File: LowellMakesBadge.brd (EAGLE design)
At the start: 50 x 50 mm, 15 parts

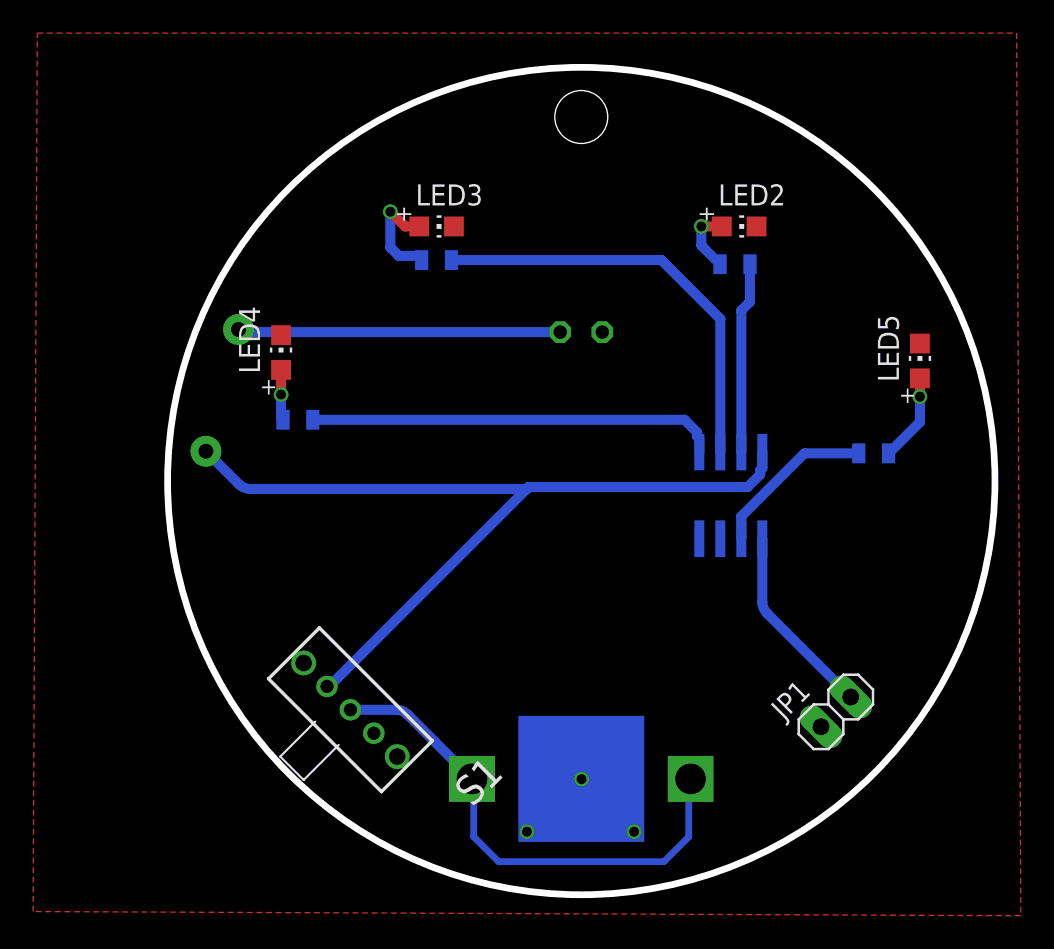
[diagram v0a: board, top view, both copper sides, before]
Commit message: Updates to use all at tiny pins (last GPIO to control main through hole LED as well
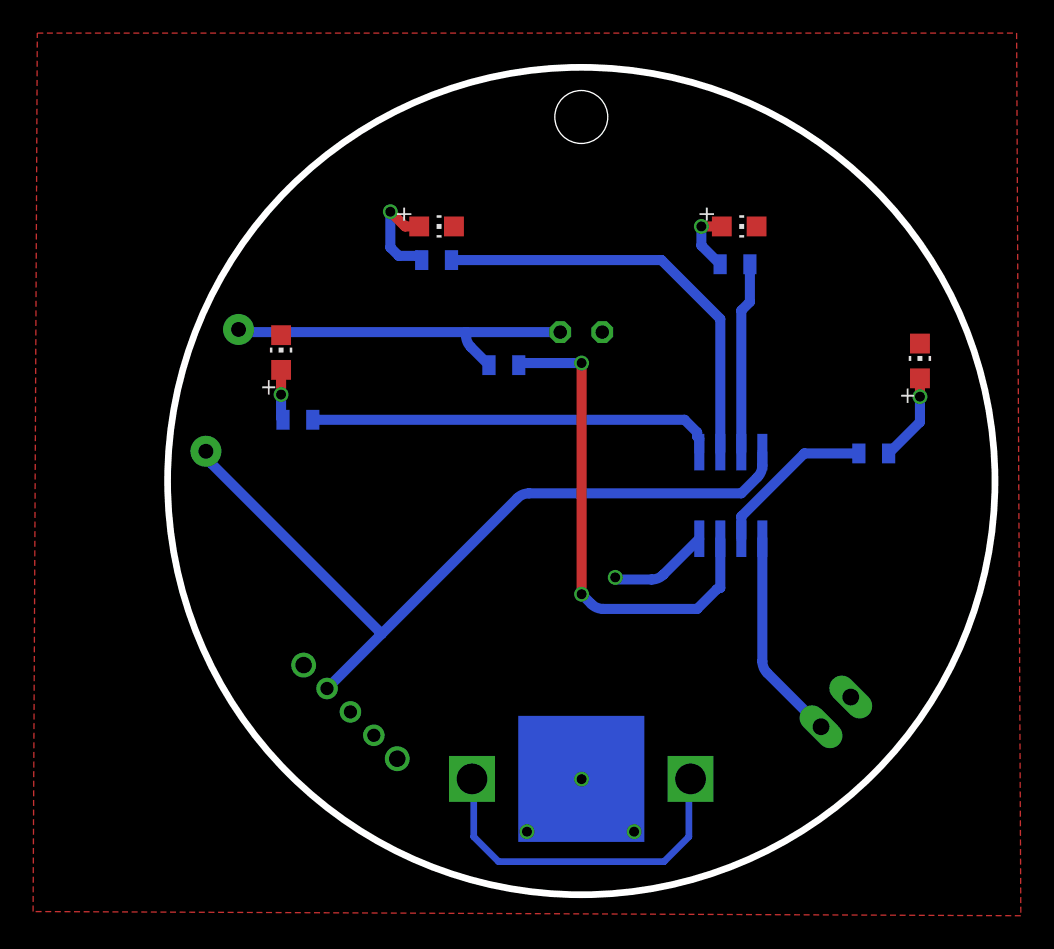
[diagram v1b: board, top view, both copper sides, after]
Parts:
- added R6: (no value), SparkFun:0805
- moved S1 0.13 mm to (11.0, 11.0), flipped to the bottom, turned to 135 degrees
- flipped JP1 to the bottom, turned to 315 degrees
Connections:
- new net N$14: R6.2, U$2.3
- net N$1: now also R6.1
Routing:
- net N$14: track 0.00 -> 30.0 mm, vias 0 -> 2
- net BATT: track 9.01 -> 0.00 mm
- net GND: track 0.00 -> 6.04 mm, vias 0 -> 4
- net VCC: track 53.1 -> 48.2 mm
- net N$1: track 19.5 -> 22.0 mm
- net RST: track 11.7 -> 12.8 mm

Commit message: Updates to wire in a full programming header.  moved SMD led pins around to simplify routing
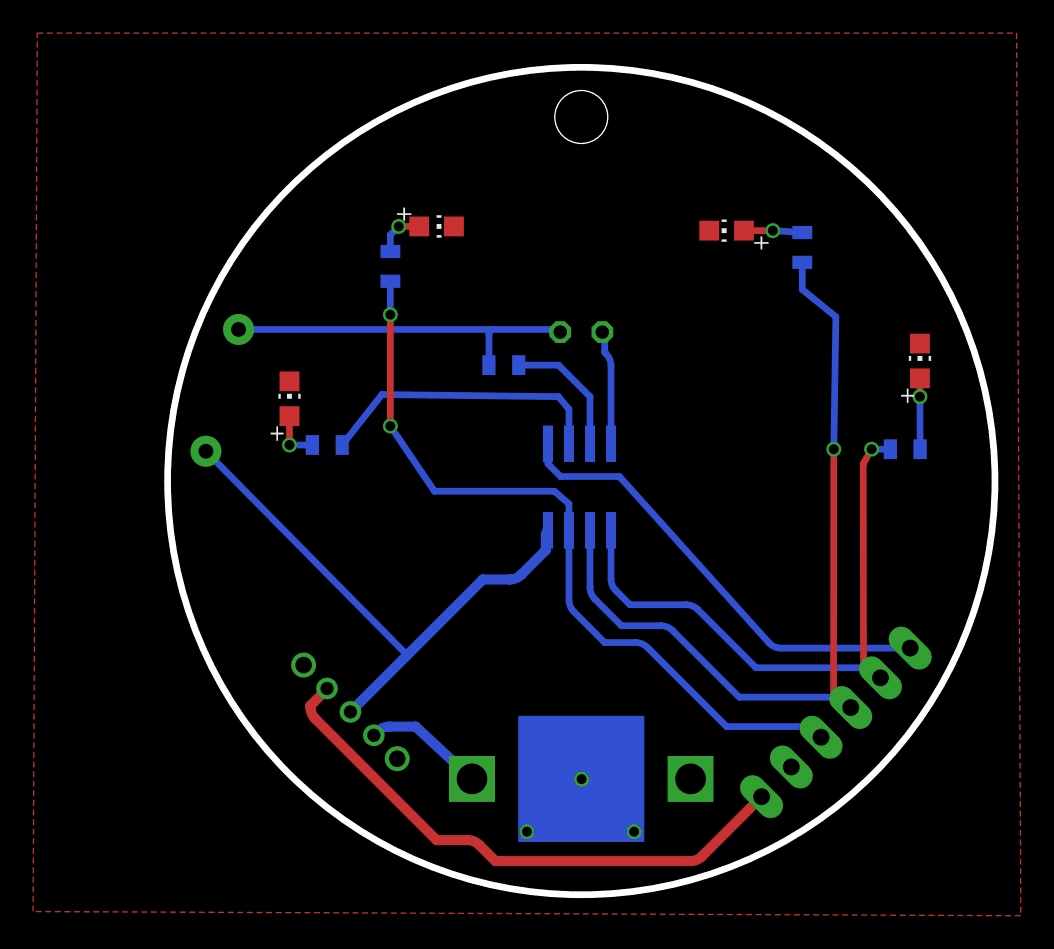
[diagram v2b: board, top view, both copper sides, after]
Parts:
- removed JP1: (no value), pinhead:1X02
- added JP2: (no value), pinhead:1X06
- moved R4 32.2 mm to (38.4, 39.1), turned to 90 degrees
- moved LED2 29.1 mm to (7.37, 30.0), turned to 0 degrees
- moved LED4 27.9 mm to (33.8, 40.1), turned to 90 degrees
- moved R2 27.0 mm to (9.65, 27.2)
- moved U$2 9.16 mm to (24.9, 24.6), turned to 180 degrees
- moved R3 2.82 mm to (13.5, 38.0), turned to 90 degrees
- moved R5 1.92 mm to (44.6, 26.9), turned to 180 degrees
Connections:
- removed net N$6 (its old number): R3.1, U$2.6
- removed net N$7: R2.1, U$2.7
- removed net N$8: R5.2, U$2.2
- removed net N$9: LED5.A, R5.1
- removed net RST: JP1.2, U$2.1
- new net N$4: LED5.A, R5.2
- new net PB0/MOSI: JP2.2, R5.1, U$2.5
- new net PB1/MISO: JP2.3, R4.1, U$2.6
- new net PB2/SCK: JP2.4, R3.1, U$2.7
- new net PROG_VCC: JP2.6, S1.3
- new net RESET: JP2.1, U$2.1
- net BATT: now also S1.1; no longer S1.2
- net GND: now also JP2.5; no longer JP1.1
- net N$5: now also R2.1, U$2.2; no longer R4.1, U$2.5
- net VCC: now also S1.2; no longer S1.3
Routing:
- net PB1/MISO: track 0.00 -> 50.7 mm, vias 0 -> 1
- net PB2/SCK: track 0.00 -> 46.4 mm, vias 0 -> 2
- net PB0/MOSI: track 0.00 -> 37.4 mm, vias 0 -> 1
- net PROG_VCC: track 0.00 -> 34.3 mm
- net RESET: track 0.00 -> 28.3 mm
- net N$6 (its old number): track 25.8 -> 0.00 mm
- net N$3: track 30.0 -> 7.94 mm, vias 2 -> 0
- net N$2: track 21.2 -> 0.00 mm
- net VCC: track 48.2 -> 34.3 mm
- net RST: track 12.8 -> 0.00 mm
- net N$7: track 11.6 -> 0.00 mm
- net N$8: track 10.0 -> 0.00 mm
- net BATT: track 0.00 -> 7.33 mm
- net N$5: track 24.8 -> 17.6 mm
- net N$9: track 5.32 -> 0.00 mm, vias 1 -> 0
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
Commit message: Cleaned up the battery power signal and passed some DRC tests
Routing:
- net N$2: track 0.00 -> 20.5 mm
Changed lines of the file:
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@@
 <wire x1="45.466" y1="30.099" x2="45.466" y2="31.208" width="0.4064" layer="1"/>
+</signal>
+<signal name="N$2">
+<wire x1="31.623" y1="6.858" x2="31.623" y2="3.9702125" width="0.6096" layer="16"/>
+<wire x1="31.623" y1="3.9702125" x2="31.33010625" y2="3.26310625" width="0.6096" layer="16" curve="-45"/>
+<wire x1="31.33010625" y1="3.26310625" x2="30.099" y2="2.032" width="0.6096" layer="16"/>
+<wire x1="30.099" y1="2.032" x2="20.0992125" y2="2.032" width="0.6096" layer="16"/>
+<wire x1="20.0992125" y1="2.032" x2="19.39210625" y2="2.32489375" width="0.6096" layer="16" curve="-45"/>
+<wire x1="19.39210625" y1="2.32489375" x2="18.288" y2="3.429" width="0.6096" layer="16"/>
+<wire x1="18.288" y1="3.429" x2="18.288" y2="6.223" width="0.6096" layer="16"/>
 </signal>
 </signals>

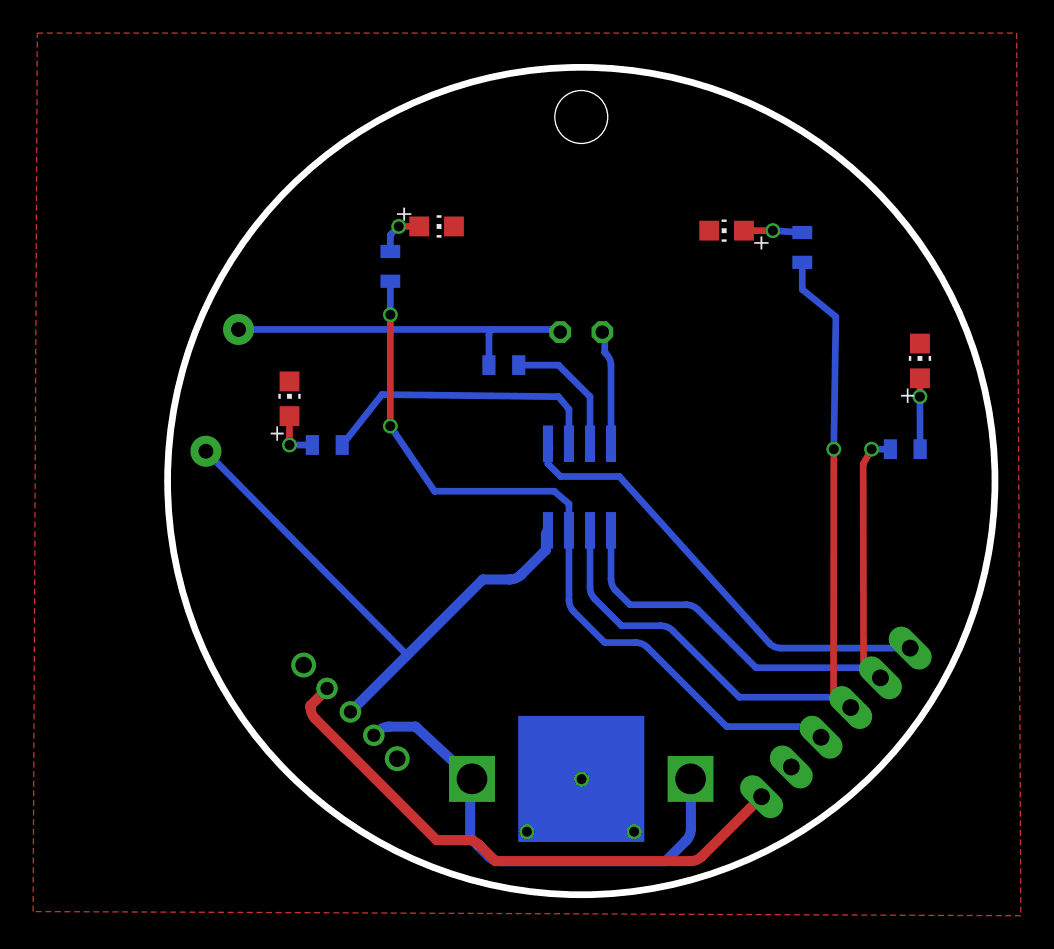
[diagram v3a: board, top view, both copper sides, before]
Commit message: Update to make board render properly in 3d model
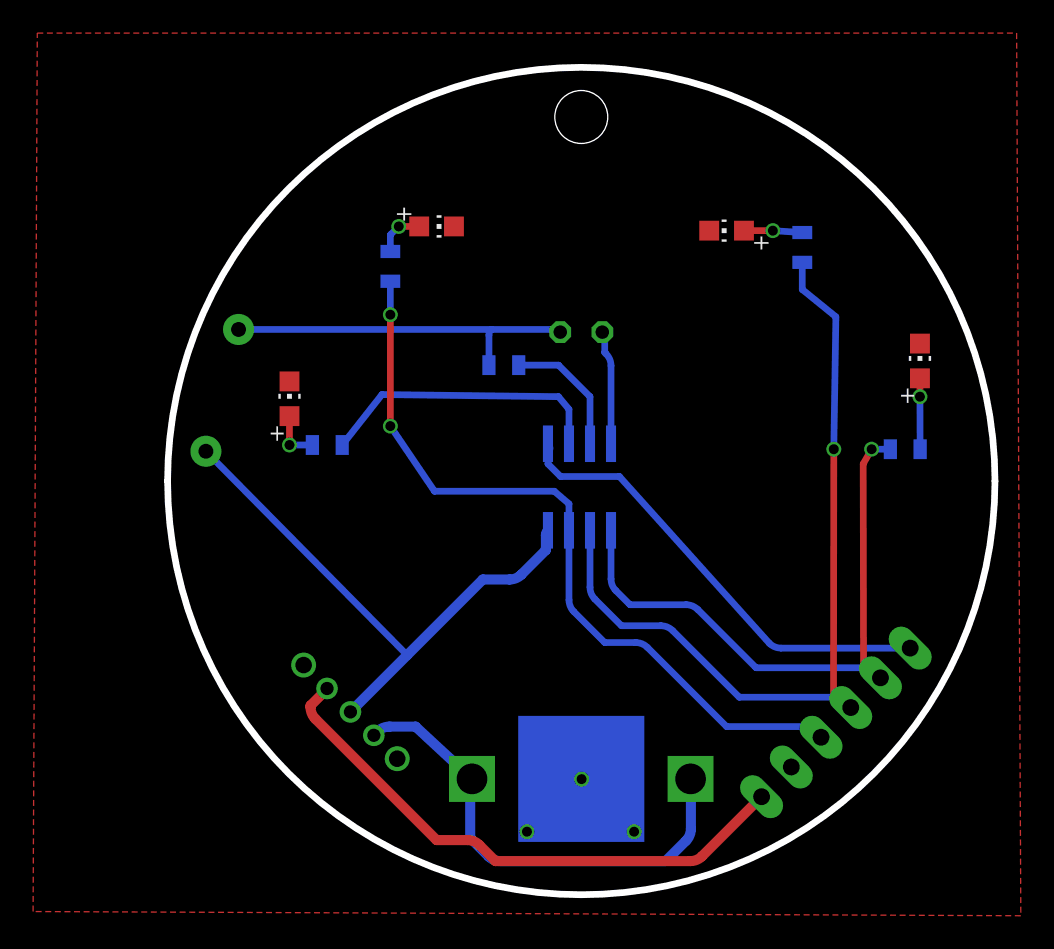
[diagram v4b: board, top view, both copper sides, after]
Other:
- outline, holes or cut-outs redrawn
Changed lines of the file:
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@@
 <setting verticaltext="up"/>
 </settings>
-<grid distance="5" unitdist="mil" unit="mil" style="lines" multiple="1" display="yes" altdistance="0.025" altunitdist="inch" altunit="inch"/>
+<grid distance="5" unitdist="mm" unit="mm" style="lines" multiple="1" display="yes" altdistance="0.025" altunitdist="inch" altunit="inch"/>
 <layers>
 <layer number="1" name="Top" color="4" fill="1" visible="yes" active="yes"/>
@@
 <layer number="220" name="220bmp" color="21" fill="1" visible="no" active="no"/>
 <layer number="221" name="221bmp" color="22" fill="1" visible="no" active="no"/>
-<layer number="222" name="222bmp" color="23" fill="1" visible="no" active="no"/>
 <layer number="223" name="223bmp" color="24" fill="1" visible="no" active="no"/>
 <layer number="224" name="224bmp" color="25" fill="1" visible="no" active="no"/>
@@
 <board>
 <plain>
-<circle x="25" y="25" radius="25" width="0.4064" layer="20"/>
 <hole x="25" y="47" drill="3.2"/>
 <text x="39.246" y="42.516" size="1.4224" layer="32" font="vector" ratio="17" rot="MR0">Lowell Makes Badge V2.0</text>
+<wire x1="0" y1="25" x2="50" y2="25" width="0.4064" layer="20" curve="-180"/>
+<wire x1="50" y1="25" x2="0" y2="25" width="0.4064" layer="20" curve="-180"/>
 </plain>
 <attributes>

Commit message: Update to name micro as U1 instead of U$2
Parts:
- renumbered U$2 to U1
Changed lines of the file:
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@@
 <attribute name="VALUE" x="21.19" y="12.08" size="0.4064" layer="28" rot="MR180"/>
 </element>
-<element name="U$2" library="LowellMakesEagleLibrary" package="SOIC8" value="ATTINY85" x="24.892" y="24.638" smashed="yes" rot="MR180">
+<element name="U1" library="LowellMakesEagleLibrary" package="SOIC8" value="ATTINY85" x="24.892" y="24.638" smashed="yes" rot="MR180">
 <attribute name="NAME" x="20.066" y="23.749" size="1.27" layer="26" rot="MR90"/>
 </element>
@@
 <wire x1="26.416" y1="32.766" x2="26.416" y2="33.647525" width="0.4064" layer="16"/>
 <wire x1="26.416" y1="33.647525" x2="26.27" y2="34" width="0.4064" layer="16" curve="45"/>
-<contactref element="U$2" pad="4"/>
+<contactref element="U1" pad="4"/>
 <wire x1="26.797" y1="31.9707875" x2="26.797" y2="27.2542" width="0.4064" layer="16"/>
 <contactref element="LED5" pad="C"/>
@@
 </signal>
 <signal name="VCC">
-<contactref element="U$2" pad="8"/>
+<contactref element="U1" pad="8"/>
 <contactref element="R1" pad="P$1"/>
 <contactref element="S1" pad="2"/>
@@
 </signal>
 <signal name="RESET">
-<contactref element="U$2" pad="1"/>
+<contactref element="U1" pad="1"/>
 <contactref element="JP2" pad="1"/>
 <wire x1="44.876128125" y1="14.904125" x2="37.0720875" y2="14.904125" width="0.4064" layer="16"/>
@@
 </signal>
 <signal name="PB0/MOSI">
-<contactref element="U$2" pad="5"/>
+<contactref element="U1" pad="5"/>
 <contactref element="JP2" pad="2"/>
 <wire x1="26.797" y1="22.0218" x2="26.797" y2="19.0832125" width="0.4064" layer="16"/>
@@
 </signal>
 <signal name="PB1/MISO">
-<contactref element="U$2" pad="6"/>
+<contactref element="U1" pad="6"/>
 <contactref element="JP2" pad="3"/>
 <wire x1="25.527" y1="22.0218" x2="25.527" y2="18.5752125" width="0.4064" layer="16"/>
@@
 </signal>
 <signal name="PB2/SCK">
-<contactref element="U$2" pad="7"/>
+<contactref element="U1" pad="7"/>
 <contactref element="JP2" pad="4"/>
 <wire x1="24.257" y1="22.0218" x2="24.257" y2="17.8132125" width="0.4064" layer="16"/>
@@
 </signal>
 <signal name="N$3">
-<contactref element="U$2" pad="3"/>
+<contactref element="U1" pad="3"/>
 <contactref element="R6" pad="2"/>
 <wire x1="25.527" y1="27.2542" x2="25.527" y2="30.099" width="0.4064" layer="16"/>
@@
 </signal>
 <signal name="N$5">
-<contactref element="U$2" pad="2"/>
+<contactref element="U1" pad="2"/>
 <contactref element="R2" pad="1"/>
 <wire x1="24.257" y1="27.2542" x2="24.257" y2="29.337" width="0.4064" layer="16"/>
